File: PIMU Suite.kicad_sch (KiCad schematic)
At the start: 11 parts, among them U2 MICROSD_SPI_OR_SDIO_CARD

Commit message: Update silk
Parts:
- R1: value R_US -> ~65Ω
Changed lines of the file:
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@@
 			)
 		)
-		(property "Description" "test point"
+		(property "Description" "GND"
 			(at 102.87 54.61 0)
 			(effects
@@
 			)
 		)
-		(property "Value" "R_US"
+		(property "Value" "~65Ω"
 			(at 147.32 30.48 90)
 			(effects
@@
 			)
 		)
-		(property "Description" ""
+		(property "Description" "ICM20649 IMU"
 			(at 231.14 76.2 0)
 			(effects
@@
 			)
 		)
-		(property "Description" "Light emitting diode"
+		(property "Description" "PWR"
 			(at 139.7 34.29 0)
 			(effects
@@
 			)
 		)
-		(property "Description" ""
+		(property "Description" "SD Card Breakout"
 			(at 67.31 83.82 0)
 			(effects

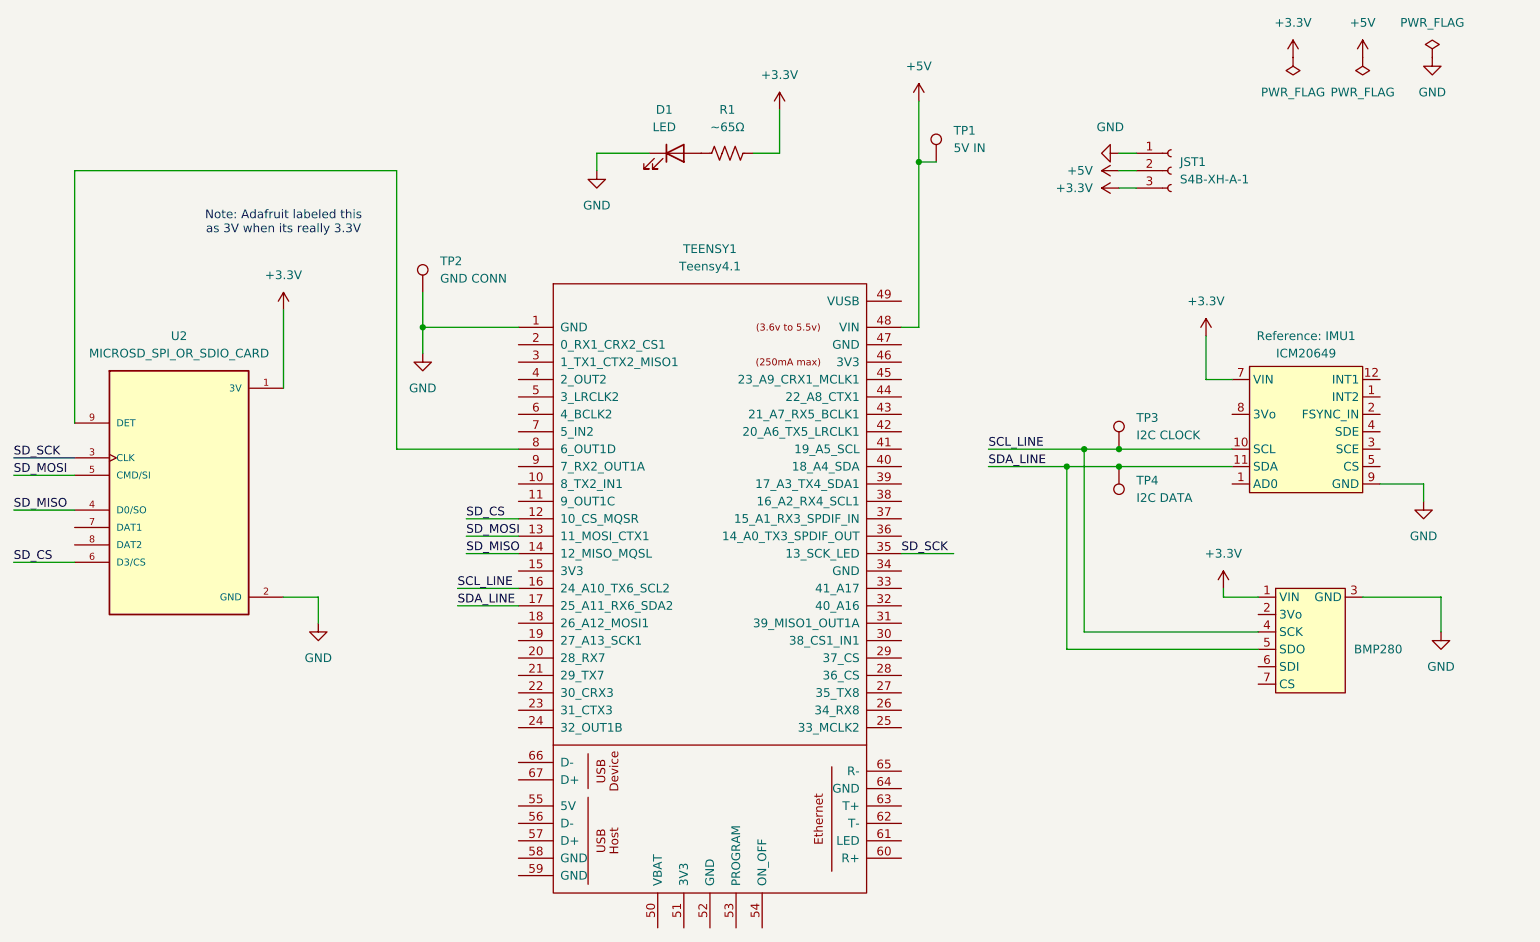
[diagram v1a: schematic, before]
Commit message: Add TE line
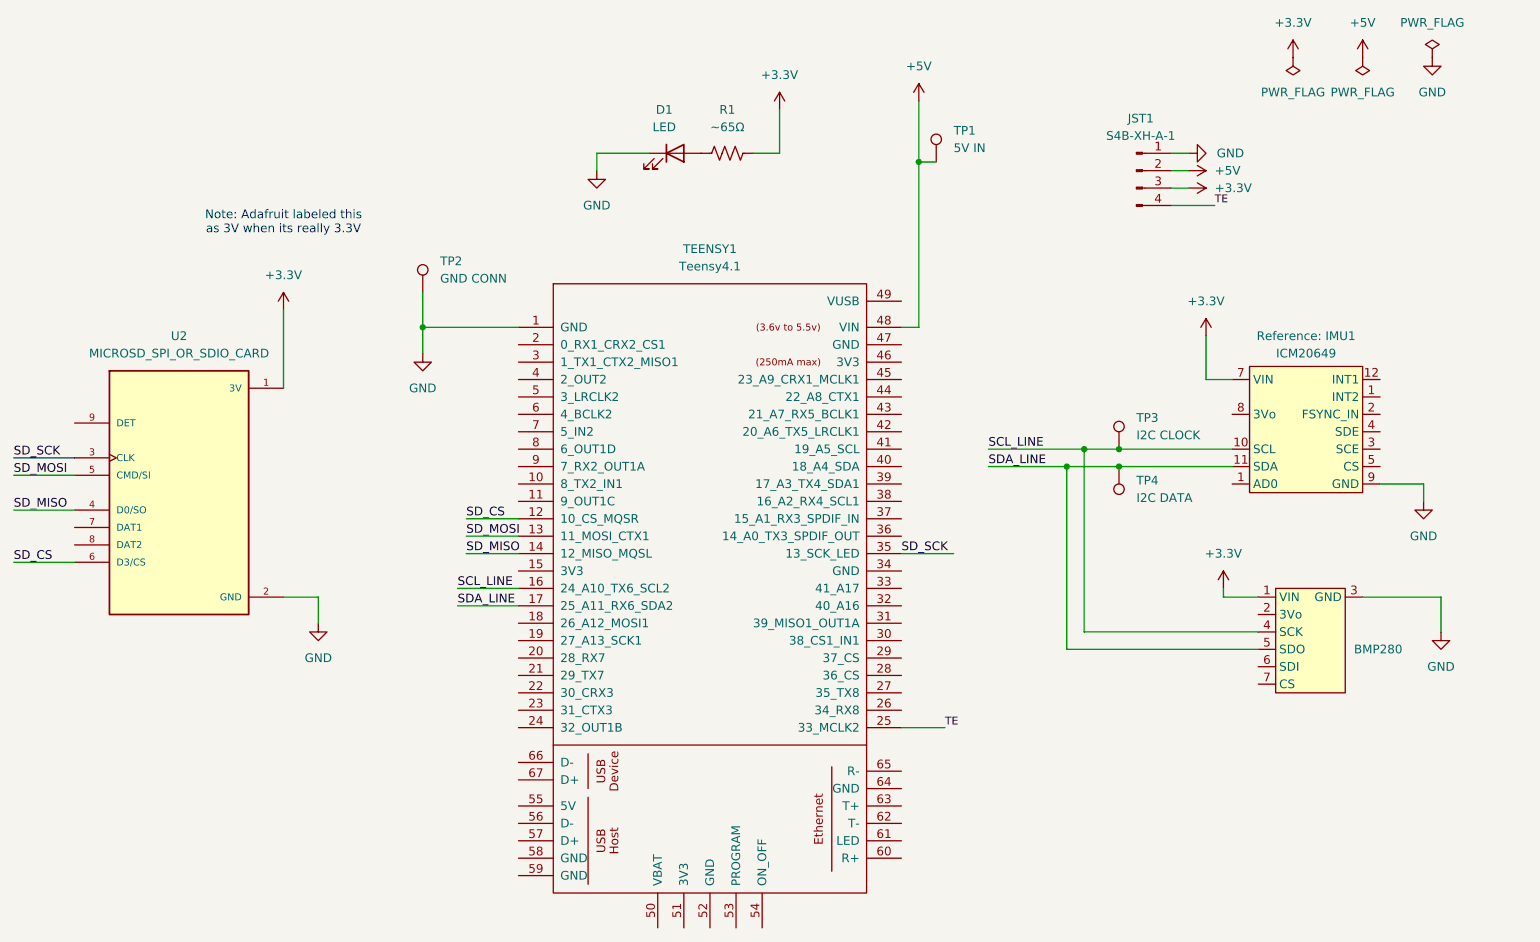
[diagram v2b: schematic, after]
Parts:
- JST1: footprint Connector_JST:JST_VH_B3P-VH-B_1x03_P3.96mm_Vertical -> Connector_JST:JST_VH_B4P-VH-B_1x04_P3.96mm_Vertical; symbol Connector:Conn_01x03_Socket -> Connector:Conn_01x04_Pin
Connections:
- net TE: now reaches TEENSY1.25 (33_MCLK2)
- net TE: now also JST1.4 (Pin_4)
- net at TEENSY1.8 (6_OUT1D): no longer U2.9 (DET)
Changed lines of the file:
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@@
-	(wire
-		(pts
-			(xy 52.07 36.83) (xy 52.07 73.66)
-		)
-		(stroke
-			(width 0)
-			(type default)
-		)
-	)
 	(wire
 		(pts
@@
 	(wire
 		(pts
-			(xy 204.47 36.83) (xy 207.01 36.83)
+			(xy 214.63 36.83) (xy 212.09 36.83)
 		)
 		(stroke
@@
 	(wire
 		(pts
+			(xy 172.72 118.11) (xy 179.07 118.11)
+		)
+		(stroke
+			(width 0)
+			(type default)
+		)
+	)
+	(wire
+		(pts
 			(xy 175.26 26.67) (xy 175.26 35.56)
 		)
@@
 	(wire
 		(pts
-			(xy 204.47 34.29) (xy 207.01 34.29)
+			(xy 214.63 39.37) (xy 212.09 39.37)
 		)
 		(stroke
@@
 	(wire
 		(pts
-			(xy 99.06 77.47) (xy 99.06 36.83)
-		)
-		(stroke
-			(width 0)
-			(type default)
-		)
-	)
-	(wire
-		(pts
 			(xy 199.39 77.47) (xy 199.39 104.14)
 		)
@@
 	(wire
 		(pts
-			(xy 99.06 36.83) (xy 52.07 36.83)
-		)
-		(stroke
-			(width 0)
-			(type default)
-		)
-	)
-	(wire
-		(pts
 			(xy 43.18 86.36) (xy 52.07 86.36)
 		)
@@
 	(wire
 		(pts
-			(xy 204.47 39.37) (xy 207.01 39.37)
+			(xy 214.63 34.29) (xy 212.09 34.29)
 		)
 		(stroke
@@
 	(wire
 		(pts
-			(xy 116.84 77.47) (xy 99.06 77.47)
+			(xy 212.09 41.91) (xy 218.44 41.91)
 		)
 		(stroke
@@
 			(width 0)
 			(type default)
+		)
+	)
+	(label "TE"
+		(at 179.07 118.11 0)
+		(effects
+			(font
+				(size 1.143 1.143)
+			)
+			(justify left bottom)
 		)
 	)
@@
 		)
 	)
+	(label "TE"
+		(at 218.44 41.91 0)
+		(effects
+			(font
+				(size 1.143 1.143)
+			)
+			(justify left bottom)
+		)
+	)
 	(label "SD_SCK"
 		(at 43.18 78.74 0)
@@
 	)
 	(symbol
-		(lib_id "Connector:Conn_01x03_Socket")
-		(at 212.09 36.83 0)
+		(lib_id "Connector:Conn_01x04_Pin")
+		(at 207.01 36.83 0)
 		(unit 1)
 		(exclude_from_sim no)
@@
 		(fields_autoplaced yes)
 		(property "Reference" "JST1"
-			(at 213.36 35.5599 0)
-			(effects
-				(font
-					(size 1.27 1.27)
-				)
-				(justify left)
+			(at 207.645 29.21 0)
+			(effects
+				(font
+					(size 1.27 1.27)
+				)
 			)
 		)
 		(property "Value" "S4B-XH-A-1"
-			(at 213.36 38.0999 0)
-			(effects
-				(font
-					(size 1.27 1.27)
-				)
-				(justify left)
-			)
-		)
-		(property "Footprint" "Connector_JST:JST_VH_B3P-VH-B_1x03_P3.96mm_Vertical"
-			(at 212.09 36.83 0)
+			(at 207.645 31.75 0)
+			(effects
+				(font
+					(size 1.27 1.27)
+				)
+			)
+		)
+		(property "Footprint" "Connector_JST:JST_VH_B4P-VH-B_1x04_P3.96mm_Vertical"
+			(at 207.01 36.83 0)
 			(effects
 				(font
@@
 		)
 		(property "Datasheet" "~"
-			(at 212.09 36.83 0)
-			(effects
-				(font
-					(size 1.27 1.27)
-				)
-				(hide yes)
-			)
-		)
-		(property "Description" "Generic connector, single row, 01x03, script generated"
-			(at 212.09 36.83 0)
+			(at 207.01 36.83 0)
+			(effects
+				(font
+					(size 1.27 1.27)
+				)
+				(hide yes)
+			)
+		)
+		(property "Description" "Generic connector, single row, 01x04, script generated"
+			(at 207.01 36.83 0)
 			(effects
 				(font
@@
 		)
 		(property "PARTREV" "27-1-20"
-			(at 212.09 36.83 0)
+			(at 207.01 36.83 0)
 			(effects
 				(font
@@
 		)
 		(property "STANDARD" "Manufacturer Recommendations"
-			(at 212.09 36.83 0)
+			(at 207.01 36.83 0)
 			(effects
 				(font
@@
 		)
 		(property "MAXIMUM_PACKAGE_HEIGHT" "6.1mm"
-			(at 212.09 36.83 0)
+			(at 207.01 36.83 0)
 			(effects
 				(font
@@
 		)
 		(property "MANUFACTURER" "JST"
-			(at 212.09 36.83 0)
+			(at 207.01 36.83 0)
 			(effects
 				(font
@@
 		)
 		(pin "1"
+		)
+		(pin "4"
 		)
 		(instances
@@
 	(symbol
 		(lib_id "power:GND")
-		(at 204.47 34.29 270)
-		(unit 1)
-		(exclude_from_sim no)
-		(in_bom yes)
-		(on_board yes)
-		(dnp no)
-		(fields_autoplaced yes)
+		(at 214.63 34.29 90)
+		(unit 1)
+		(exclude_from_sim no)
+		(in_bom yes)
+		(on_board yes)
+		(dnp no)
 		(property "Reference" "#PWR06"
-			(at 198.12 34.29 0)
+			(at 220.98 34.29 0)
 			(effects
 				(font
@@
 		)
 		(property "Value" "GND"
-			(at 203.2 30.48 90)
+			(at 220.726 34.29 90)
 			(effects
 				(font
@@
 		)
 		(property "Footprint" ""
-			(at 204.47 34.29 0)
+			(at 214.63 34.29 0)
 			(effects
 				(font
@@
 		)
 		(property "Datasheet" ""
-			(at 204.47 34.29 0)
+			(at 214.63 34.29 0)
 			(effects
 				(font
@@
 		)
 		(property "Description" "Power symbol creates a global label with name \"GND\" , ground"
-			(at 204.47 34.29 0)
+			(at 214.63 34.29 0)
 			(effects
 				(font
@@
 	(symbol
 		(lib_id "power:+3.3V")
-		(at 204.47 39.37 90)
+		(at 214.63 39.37 270)
 		(unit 1)
 		(exclude_from_sim no)
@@
 		(fields_autoplaced yes)
 		(property "Reference" "#PWR011"
-			(at 208.28 39.37 0)
+			(at 210.82 39.37 0)
 			(effects
 				(font
@@
 		)
 		(property "Value" "+3.3V"
-			(at 200.66 39.3699 90)
+			(at 218.44 39.3701 90)
 			(effects
 				(font
@@
 		)
 		(property "Footprint" ""
-			(at 204.47 39.37 0)
+			(at 214.63 39.37 0)
 			(effects
 				(font
@@
 		)
 		(property "Datasheet" ""
-			(at 204.47 39.37 0)
+			(at 214.63 39.37 0)
 			(effects
 				(font
@@
 		)
 		(property "Description" "Power symbol creates a global label with name \"+3.3V\""
-			(at 204.47 39.37 0)
+			(at 214.63 39.37 0)
 			(effects
 				(font
@@
 	(symbol
 		(lib_id "power:+5V")
-		(at 204.47 36.83 90)
+		(at 214.63 36.83 270)
 		(unit 1)
 		(exclude_from_sim no)
@@
 		(fields_autoplaced yes)
 		(property "Reference" "#PWR012"
-			(at 208.28 36.83 0)
+			(at 210.82 36.83 0)
 			(effects
 				(font
@@
 		)
 		(property "Value" "+5V"
-			(at 200.66 36.8299 90)
+			(at 218.44 36.8301 90)
 			(effects
 				(font
@@
 		)
 		(property "Footprint" ""
-			(at 204.47 36.83 0)
+			(at 214.63 36.83 0)
 			(effects
 				(font
@@
 		)
 		(property "Datasheet" ""
-			(at 204.47 36.83 0)
+			(at 214.63 36.83 0)
 			(effects
 				(font
@@
 		)
 		(property "Description" "Power symbol creates a global label with name \"+5V\""
-			(at 204.47 36.83 0)
-			(effects
-				(font
+			(at 214.63 36.83 0)
+			(effects
+				(font

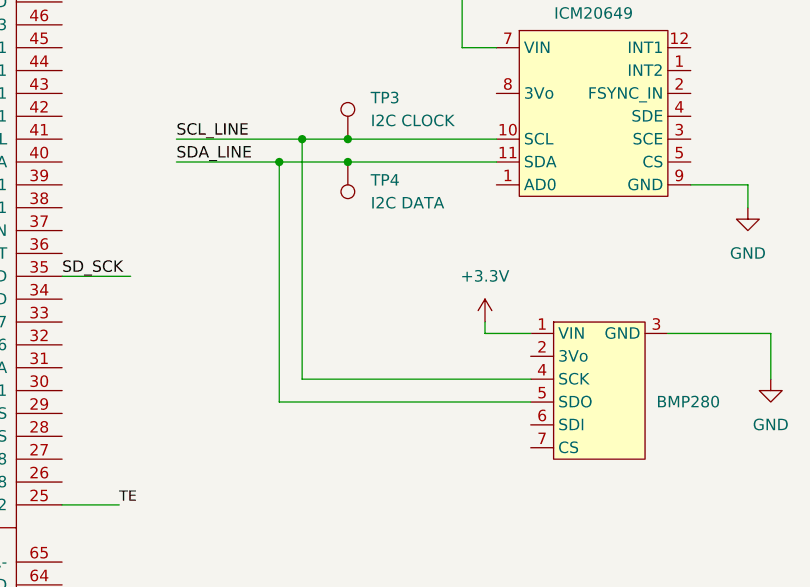
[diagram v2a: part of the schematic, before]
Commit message: Fix wrong wiring
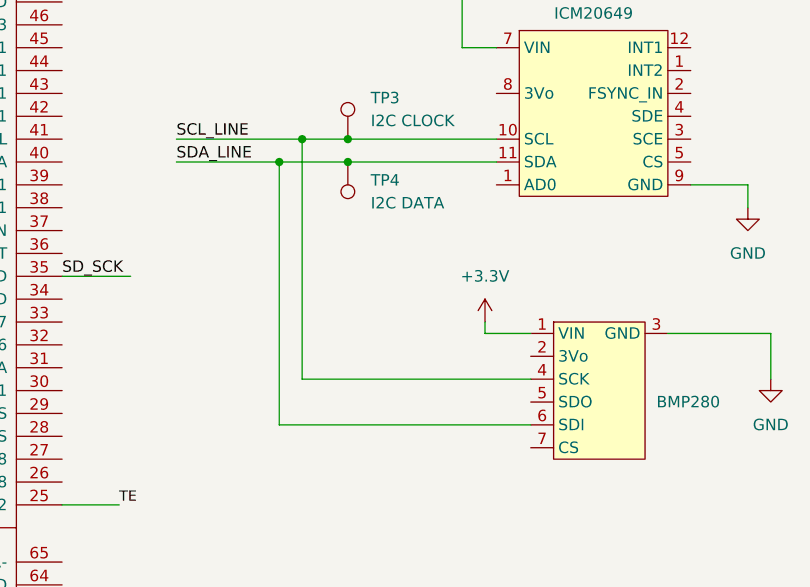
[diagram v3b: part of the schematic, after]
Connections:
- net SDA_LINE: now also BMP1.6 (SDI); no longer BMP1.5 (SDO)
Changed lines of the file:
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@@
-	(wire
-		(pts
-			(xy 196.85 106.68) (xy 224.79 106.68)
-		)
-		(stroke
-			(width 0)
-			(type default)
-		)
-	)
-	(wire
-		(pts
-			(xy 196.85 80.01) (xy 196.85 106.68)
-		)
-		(stroke
-			(width 0)
-			(type default)
-		)
-	)
 	(wire
 		(pts
@@
 		)
 		(stroke
+			(width 0)
+			(type default)
+		)
+	)
+	(wire
+		(pts
+			(xy 196.85 80.01) (xy 196.85 109.22)
+		)
+		(stroke
+			(width 0)
+			(type default)
+		)
+	)
+	(wire
+		(pts
+			(xy 224.79 109.22) (xy 196.85 109.22)
+		)
+		(stroke

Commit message: JLCPCB specs
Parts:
- JST1: value S4B-XH-A-1 -> JST_VH_B4P-VH-B
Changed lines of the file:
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@@
 			)
 		)
-		(property "Value" "S4B-XH-A-1"
+		(property "Value" "JST_VH_B4P-VH-B"
 			(at 207.645 31.75 0)
 			(effects

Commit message: tx rx
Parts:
- added TP5: 3V3, TestPoint:TestPoint_Pad_D1.5mm, symbol Connector:TestPoint
- added TP6: TE, TestPoint:TestPoint_Pad_D1.5mm, symbol Connector:TestPoint
- added TP7: TX, TestPoint:TestPoint_Pad_D1.5mm, symbol Connector:TestPoint
- added TP8: RX, TestPoint:TestPoint_Pad_D1.5mm, symbol Connector:TestPoint
- JST1: value JST_VH_B4P-VH-B -> JST_VH_B6P-VH-B; footprint Connector_JST:JST_VH_B4P-VH-B_1x04_P3.96mm_Vertical -> Connector_JST:JST_VH_B6P-VH-B_1x06_P3.96mm_Vertical; symbol Connector:Conn_01x04_Pin -> Connector:Conn_01x06_Pin
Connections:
- net +3.3V: now also TP5.1
- net TE: now also TP6.1
- net UART_TO_TEENSY: now reaches TEENSY1.26 (34_RX8)
- net UART_TO_TEENSY: now also JST1.5 (Pin_5), TP8.1
- net UART_FROM_TEENSY: now reaches TEENSY1.27 (35_TX8)
- net UART_FROM_TEENSY: now also JST1.6 (Pin_6), TP7.1
